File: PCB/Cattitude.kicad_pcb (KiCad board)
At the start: 2 copper layers, 15 parts, among them J1 Conn_01x08_Pin, J2 Conn_01x04_Pin, J3 Conn_01x02_Pin, J4 Conn_01x02_Pin, J5 Conn_01x03_Pin, J6 Conn_01x03_Pin, J7 Conn_01x03_Pin, J8 Conn_01x03_Pin, SW2 SW_SPDT, U1 102010551

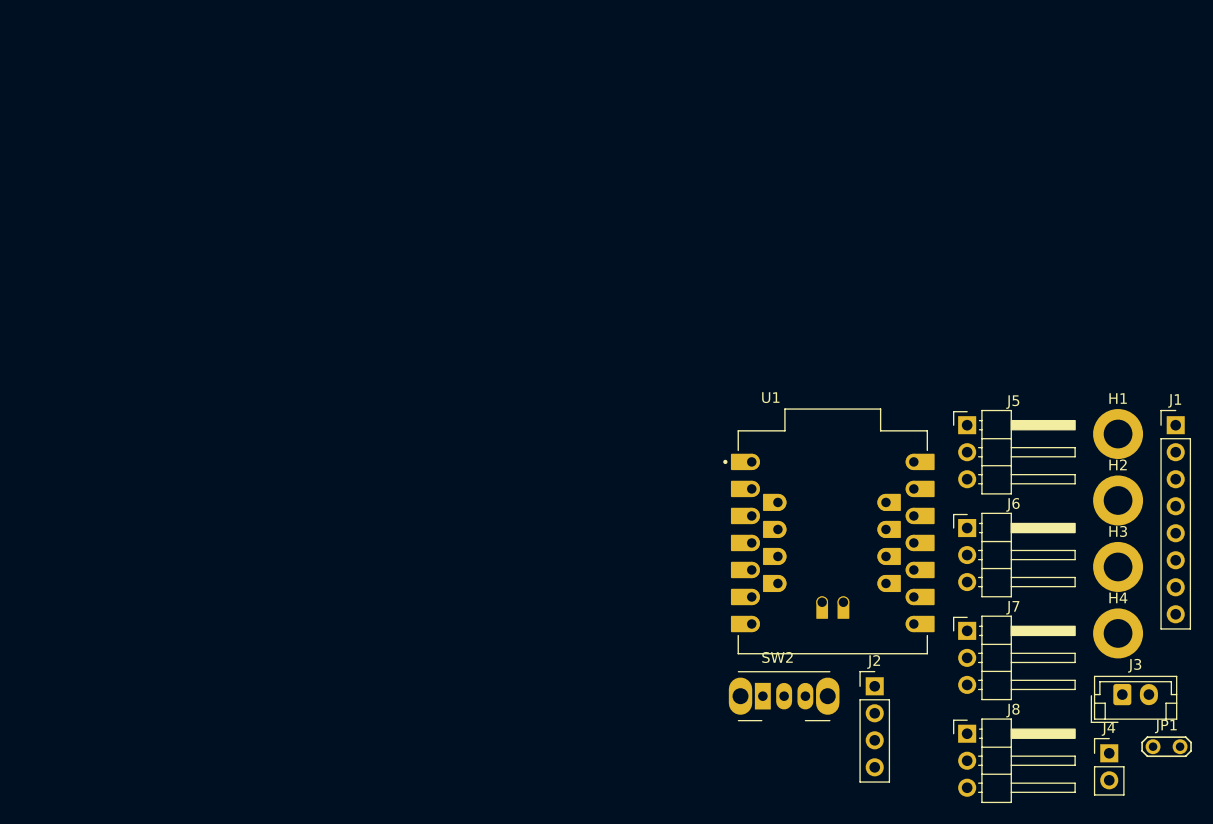
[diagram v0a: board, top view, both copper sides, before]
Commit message: PCB Routing done
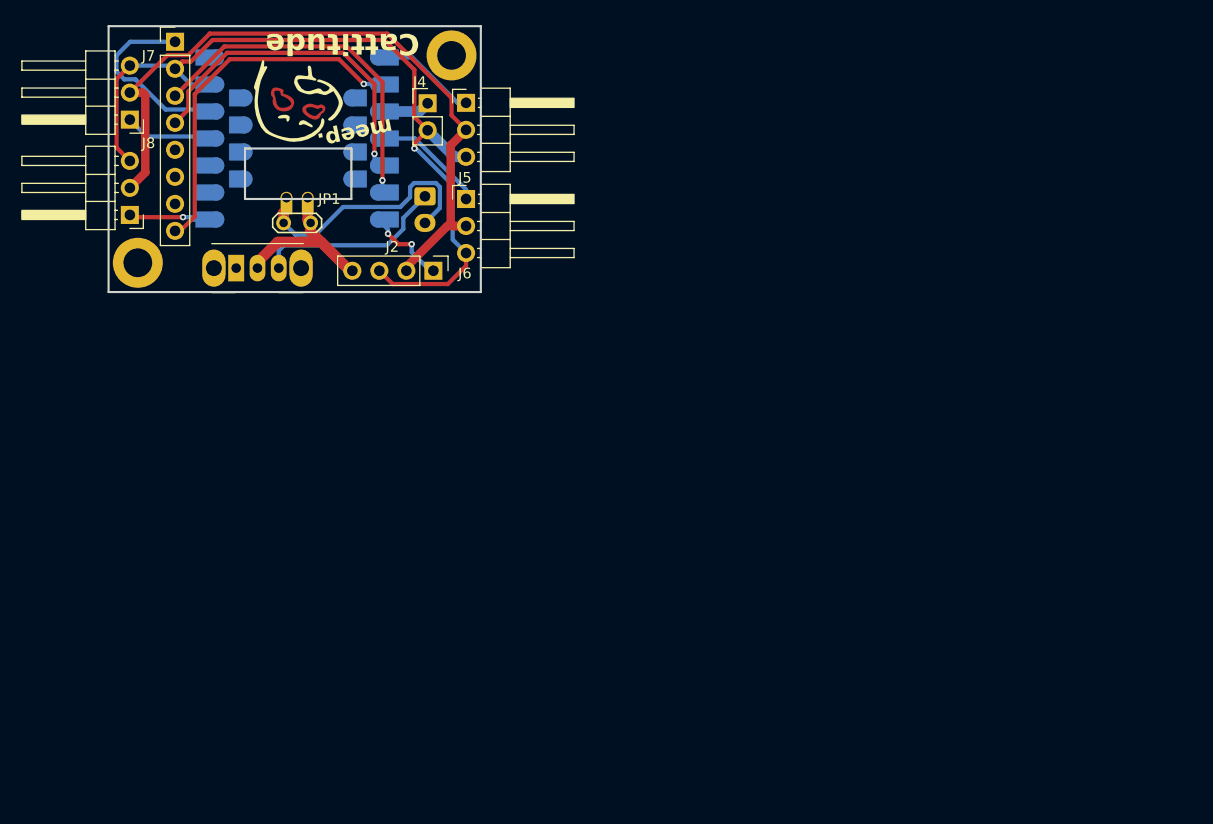
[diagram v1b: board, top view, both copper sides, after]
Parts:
- removed H3, H4: MountingHole, MountingHole:MountingHole_2.7mm_M2.5_DIN965_Pad
- added G***: LOGO, LOGO, F.Cu at (42.8, 32.2)
- J1: footprint Connector_PinHeader_2.54mm:PinHeader_1x08_P2.54mm_Vertical -> CustomParts:MPU 6050
- J3, U1: moved to B.Cu
- moved J1 102.6 mm to (29.8, 25.0)
- moved H2 94.8 mm to (27.8, 47.2)
- moved JP1 93.3 mm to (44.0, 43.5), turned to 180 degrees
- moved J8 92.6 mm to (27.0, 42.8), turned to 180 degrees
- moved J7 92.2 mm to (27.0, 33.8), turned to 180 degrees
- moved J4 88.6 mm to (55.0, 32.2)
- moved J3 80.6 mm to (54.8, 41.0), turned to -90 degrees
- moved H1 72.1 mm to (57.2, 27.8)
- moved SW2 63.8 mm to (37.0, 47.8)
- moved U1 63.1 mm to (42.7, 35.6), turned to 180 degrees
- moved J2 57.0 mm to (55.5, 48.0), turned to -90 degrees
- moved J6 56.4 mm to (58.6, 41.2)
- moved J5 56.0 mm to (58.6, 32.2)
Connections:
- U1 pad 11: unconnected-(U1-D10/P109/CTX0/SPI9_MOSI-Pad11) -> SERVO_D3
- U1 pad 3: SERVO_D2 -> HAPTIC_MOTOR
- U1 pad 4: SERVO_D3 -> SERVO_D2
- U1 pad 7: SERVO_D4 -> SERVO_EN
- U1 pad 8: HAPTIC_MOTOR -> SERVO_D4
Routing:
- net GND: track 0.00 -> 79.2 mm, vias 0 -> 1
- net SERVO_5V: track 0.00 -> 68.0 mm
- net INT: track 0.00 -> 33.5 mm, vias 0 -> 1
- net SCL: track 0.00 -> 33.4 mm, vias 0 -> 1
- net SDA: track 0.00 -> 31.5 mm, vias 0 -> 1
- net -BATT: track 0.00 -> 23.2 mm
- net +BATT: track 0.00 -> 19.2 mm
- net +3.3V: track 0.00 -> 18.5 mm
- net Net-(J3-Pin_1): track 0.00 -> 18.1 mm
- net SERVO_D2: track 0.00 -> 11.1 mm
- net SERVO_D1: track 0.00 -> 10.0 mm
- net SERVO_D3: track 0.00 -> 8.84 mm
- net SERVO_D4: track 0.00 -> 8.29 mm, vias 0 -> 1
- net SERVO_EN: track 0.00 -> 7.87 mm, vias 0 -> 2
- net HAPTIC_MOTOR: track 0.00 -> 4.97 mm
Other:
- board outline added: 35 x 25 mm
- board text added: "Cattitude"
- board text added: "Logan Peterson"
- board text added: "meep."
